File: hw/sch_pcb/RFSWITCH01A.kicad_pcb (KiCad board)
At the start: 2 copper layers, 40.1 x 40.1 mm, 31 parts, among them J1 HEADER_2x03_PARALLEL, J10 SMA, J11 HEADER_2x01_PARALLEL, J12 HEADER_2x01_PARALLEL, J2 HEADER_2x01_PARALLEL, J3 SMA, J4 SMA, J5 HEADER_2x01_PARALLEL, J6 HEADER_2x01_PARALLEL, J7 HEADER_2x01_PARALLEL, J8 HEADER_2x01_PARALLEL, J9 SMA, M1 HOLE, M2 HOLE, M3 HOLE, M4 HOLE, U1 TPS22945DCKR, U2 SPF5189Z, U3 PE4259, U4 PE4259

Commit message: Edit PCB
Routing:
- net GND: track 0.00 -> 2.03 mm
- net (no net): track 2.03 -> 0.00 mm
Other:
- board text added: "IN 3V3"
- board text added: "POWER"
- board text added: "RX/TX1"
- board text added: "RX/TX2"
- board text removed: "POWER IN"
- board text removed: "RX/TX-1"
- board text removed: "RX/TX-2"
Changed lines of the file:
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@@
     (pad "2" thru_hole circle (at -2.54 -2.54) (size 2.74 2.74) (drill 1.7) (layers *.Cu *.Mask)
       (net 2 "GND"))
-    (model "${KISYS3DMOD}/Connector_Coaxial.3dshapes/SMB_Jack_Vertical.wrl"
-      (offset (xyz 0 0 0))
+    (model "${KISYS3DMOD_MLAB}/MCX_TE_1330126-1_Vertical.step"
+      (offset (xyz 0 0 5.2))
       (scale (xyz 1 1 1))
       (rotate (xyz 0 0 0))
@@
     (property "Sheet name" "")
     (attr through_hole)
-    (fp_text reference "J3" (at -5.08 -0.635 90) (layer "F.SilkS")
+    (fp_text reference "J3" (at -5.08 0 90) (layer "F.SilkS")
       (effects (font (size 1 1) (thickness 0.15)))
     )
@@
     (pad "2" thru_hole circle (at 2.54 -2.54) (size 2.74 2.74) (drill 1.7) (layers *.Cu *.Mask)
       (net 2 "GND"))
-    (model "${KISYS3DMOD}/Connector_Coaxial.3dshapes/SMB_Jack_Vertical.wrl"
-      (offset (xyz 0 0 0))
+    (model "${KISYS3DMOD_MLAB}/MCX_TE_1330126-1_Vertical.step"
+      (offset (xyz 0 0 5.2))
       (scale (xyz 1 1 1))
       (rotate (xyz 0 0 0))
@@
     (pad "2" thru_hole circle (at -2.54 -2.54) (size 2.74 2.74) (drill 1.7) (layers *.Cu *.Mask)
       (net 2 "GND"))
-    (model "${KISYS3DMOD}/Connector_Coaxial.3dshapes/SMB_Jack_Vertical.wrl"
-      (offset (xyz 0 0 0))
+    (model "${KISYS3DMOD_MLAB}/MCX_TE_1330126-1_Vertical.step"
+      (offset (xyz 0 0 5.2))
       (scale (xyz 1 1 1))
       (rotate (xyz 0 0 0))
@@
     (property "Sheet name" "")
     (attr through_hole)
-    (fp_text reference "J4" (at -5.08 1 90) (layer "F.SilkS")
+    (fp_text reference "J4" (at -5.08 0 90) (layer "F.SilkS")
       (effects (font (size 1 1) (thickness 0.15)))
     )
@@
     (pad "2" thru_hole circle (at 2.54 2.54) (size 2.74 2.74) (drill 1.7) (layers *.Cu *.Mask)
       (net 2 "GND"))
-    (model "${KISYS3DMOD}/Connector_Coaxial.3dshapes/SMB_Jack_Vertical.wrl"
-      (offset (xyz 0 0 0))
+    (model "${KISYS3DMOD_MLAB}/MCX_TE_1330126-1_Vertical.step"
+      (offset (xyz 0 0 5.2))
       (scale (xyz 1 1 1))
       (rotate (xyz 0 0 0))
@@
   )
   (gr_line (start 28.702 -12.7) (end 28.956 -12.446) (layer "F.SilkS") (width 0.15))
-  (gr_line (start 13.335 -23.495) (end 13.97 -22.86) (layer "F.SilkS") (width 0.15))
   (gr_line (start 9.8552 -14.605) (end 11.663391 -14.605) (layer "F.SilkS") (width 0.15))
   (gr_line (start 15.387609 -14.605) (end 19.791391 -14.605) (layer "F.SilkS") (width 0.15))
+  (gr_line (start 11.663391 -14.605) (end 10.795 -15.24) (layer "F.SilkS") (width 0.15))
   (gr_circle (center 14.986 -14.605) (end 15.113 -14.986) (layer "F.SilkS") (width 0.15))
   (gr_line (start 20.066 -10.668) (end 20.066 -12.7) (layer "F.SilkS") (width 0.15))
   (gr_line (start 9.8552 -26.035) (end 11.43 -26.035) (layer "F.SilkS") (width 0.15))
   (gr_circle (center 22.098 -17.145) (end 22.352 -17.526) (layer "F.SilkS") (width 0.15))
+  (gr_line (start 13.97 -24.13) (end 13.335 -23.495) (layer "F.SilkS") (width 0.15))
   (gr_line (start 11.43 -19.05) (end 16.51 -19.05) (layer "F.SilkS") (width 0.15))
   (gr_circle (center 20.193 -14.605) (end 20.32 -14.986) (layer "F.SilkS") (width 0.15))
   (gr_line (start 27.686 -12.446) (end 27.686 -13.208) (layer "F.SilkS") (width 0.15))
-  (gr_line (start 10.795 -26.67) (end 11.43 -26.035) (layer "F.SilkS") (width 0.15))
+  (gr_line (start 13.97 -19.05) (end 14.605 -18.326453) (layer "F.SilkS") (width 0.15))
   (gr_line (start 14.986 -14.605) (end 12.446 -16.256) (layer "F.SilkS") (width 0.15))
   (gr_line (start 22.86 -11.938) (end 22.098 -12.7) (layer "F.SilkS") (width 0.15))
   (gr_circle (center 13.97 -17.145) (end 14.224 -17.526) (layer "F.SilkS") (width 0.15))
   (gr_line (start 13.97 -24.13) (end 13.97 -22.86) (layer "F.SilkS") (width 0.15))
-  (gr_line (start 1.016 -22.86) (end 1.016 -25.4) (layer "F.SilkS") (width 0.15))
+  (gr_line (start 13.97 -19.05) (end 13.335 -18.326453) (layer "F.SilkS") (width 0.15))
   (gr_line (start 11.43 -22.86) (end 11.43 -19.05) (layer "F.SilkS") (width 0.15))
   (gr_line (start 29.718 -11.684) (end 29.718 -10.922) (layer "F.SilkS") (width 0.15))
-  (gr_line (start 1.016 -25.4) (end 1.524 -25.908) (layer "F.SilkS") (width 0.15))
+  (gr_line (start 10.795 -15.24) (end 11.663391 -14.605) (layer "F.SilkS") (width 0.15))
+  (gr_line (start 13.97 -24.13) (end 14.605 -23.495) (layer "F.SilkS") (width 0.15))
   (gr_line (start 22.86 -26.035) (end 22.098 -25.273) (layer "F.SilkS") (width 0.15))
   (gr_line (start 22.098 -25.273) (end 22.098 -24.13) (layer "F.SilkS") (width 0.15))
   (gr_line (start 22.098 -12.7) (end 14.732 -12.7) (layer "F.SilkS") (width 0.15))
-  (gr_line (start 13.97 -22.86) (end 14.605 -23.495) (layer "F.SilkS") (width 0.15))
-  (gr_line (start 1.016 -17.78) (end 1.016 -15.24) (layer "F.SilkS") (width 0.15))
-  (gr_line (start 10.795 -25.4) (end 11.43 -26.035) (layer "F.SilkS") (width 0.15))
+  (gr_line (start 11.663391 -14.605) (end 10.795 -13.97) (layer "F.SilkS") (width 0.15))
   (gr_line (start 29.718 -11.684) (end 28.956 -12.446) (layer "F.SilkS") (width 0.15))
   (gr_circle (center 23.114 -14.605) (end 23.241 -14.986) (layer "F.SilkS") (width 0.15))
@@
   (gr_line (start 16.51 -19.05) (end 16.51 -22.86) (layer "F.SilkS") (width 0.15))
   (gr_line (start 13.97 -12.954) (end 13.97 -13.462) (layer "F.SilkS") (width 0.15))
-  (gr_line (start 11.43 -26.035) (end 10.795 -26.67) (layer "F.SilkS") (width 0.15))
   (gr_line (start 16.51 -27.94) (end 11.43 -27.94) (layer "F.SilkS") (width 0.15))
-  (gr_line (start 1.524 -14.732) (end 2.032 -14.732) (layer "F.SilkS") (width 0.15))
   (gr_line (start 22.606 -13.97) (end 22.098 -13.97) (layer "F.SilkS") (width 0.15))
   (gr_line (start 13.97 -13.462) (end 13.97 -12.954) (layer "F.SilkS") (width 0.15))
@@
   (gr_line (start 23.114 -16.256) (end 20.193 -14.605) (layer "F.SilkS") (width 0.15))
   (gr_line (start 26.416 -13.208) (end 22.86 -13.208) (layer "F.SilkS") (width 0.15))
-  (gr_line (start 1.524 -25.908) (end 2.032 -25.908) (layer "F.SilkS") (width 0.15))
   (gr_line (start 22.86 -13.208) (end 22.098 -13.97) (layer "F.SilkS") (width 0.15))
   (gr_line (start 16.51 -22.86) (end 11.43 -22.86) (layer "F.SilkS") (width 0.15))
+  (gr_line (start 9.8552 -26.035) (end 10.6426 -26.67) (layer "F.SilkS") (width 0.15))
   (gr_line (start 16.51 -24.13) (end 16.51 -27.94) (layer "F.SilkS") (width 0.15))
-  (gr_line (start 13.97 -22.86) (end 13.335 -23.495) (layer "F.SilkS") (width 0.15))
+  (gr_line (start 9.8552 -26.035) (end 10.6426 -25.4) (layer "F.SilkS") (width 0.15))
   (gr_line (start 11.43 -24.13) (end 16.51 -24.13) (layer "F.SilkS") (width 0.15))
   (gr_line (start 11.43 -27.94) (end 11.43 -24.13) (layer "F.SilkS") (width 0.15))
   (gr_line (start 30.7848 -26.035) (end 22.86 -26.035) (layer "F.SilkS") (width 0.15))
-  (gr_line (start 1.016 -15.24) (end 1.524 -14.732) (layer "F.SilkS") (width 0.15))
   (gr_line (start 28.702 -12.7) (end 28.194 -13.208) (layer "F.SilkS") (width 0.15))
   (gr_line (start 22.098 -13.97) (end 22.098 -13.462) (layer "F.SilkS") (width 0.15))
@@
     (effects (font (size 1.5 1.5) (thickness 0.3)) (justify mirror))
   )
-  (gr_text "RX/TX-1" (at 34.29 -31.369) (layer "F.SilkS")
+  (gr_text "RX/TX1" (at 34.29 -31.369) (layer "F.SilkS")
     (effects (font (size 1.5 1.5) (thickness 0.3)))
   )
@@
     (effects (font (size 1.5 1.5) (thickness 0.3)))
   )
-  (gr_text "3V3" (at 13.208 -1.27) (layer "F.SilkS")
+  (gr_text "IN 3V3" (at 13.208 -1.27) (layer "F.SilkS")
     (effects (font (size 1.5 1.5) (thickness 0.3)))
   )
@@
     (effects (font (size 1.5 1.5) (thickness 0.3)))
   )
-  (gr_text "POWER IN" (at 13.208 -8.89) (layer "F.SilkS")
+  (gr_text "POWER" (at 13.208 -8.89) (layer "F.SilkS")
     (effects (font (size 1.5 1.5) (thickness 0.3)))
   )
@@
     (effects (font (size 1.5 1.5) (thickness 0.3)))
   )
-  (gr_text "RFSWITCH01A" (at -2.159 -23.876 90) (layer "F.SilkS")
+  (gr_text "RFSWITCH01A" (at 20.32 -26.035 90) (layer "F.SilkS")
     (effects (font (size 1.5 1.5) (thickness 0.3)))
   )
@@
     (effects (font (size 1.5 1.5) (thickness 0.3)))
   )
-  (gr_text "RX/TX-2" (at 33.909 -20.32) (layer "F.SilkS")
+  (gr_text "RX/TX2" (at 34.29 -20.32) (layer "F.SilkS")
     (effects (font (size 1.5 1.5) (thickness 0.3)))
   )
@@
     (effects (font (size 1.5 1.5) (thickness 0.3)))
   )
-  (gr_text "MLAB.CZ" (at -5.207 -26.416 90) (layer "F.SilkS")
+  (gr_text "MLAB.CZ" (at 17.78 -26.67 90) (layer "F.SilkS")
     (effects (font (size 1.5 1.5) (thickness 0.3)))
   )
@@
     (effects (font (size 1.5 1.5) (thickness 0.3)))
   )
-  (segment (start 15.24 -12.192) (end 17.272 -12.192) (width 0.25) (layer "F.Cu") (net 0))
   (segment (start 13.208 -7.493) (end 13.42701 -7.71201) (width 0.8) (layer "F.Cu") (net 1))
   (segment (start 13.42701 -7.71201) (end 13.97 -8.255) (width 0.8) (layer "F.Cu") (net 1))
@@
   (segment (start 12.065 -11.43) (end 13.97 -11.43) (width 0.8) (layer "B.Cu") (net 1))
   (segment (start 17.78 -34.29) (end 17.78 -36.83) (width 0.4) (layer "B.Cu") (net 1))
+  (segment (start 15.24 -12.192) (end 17.272 -12.192) (width 0.25) (layer "F.Cu") (net 2))
   (via (at 11.049 -27.432) (size 0.4) (drill 0.15) (layers "F.Cu" "B.Cu") (net 2))
   (via (at 24.384 -21.844) (size 0.4) (drill 0.15) (layers "F.Cu" "B.Cu") (net 2))

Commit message: Předělávání PCB
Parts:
- removed J12: HEADER_2x01_PARALLEL, Mlab_Pin_Headers:Straight_2x01
- removed the J2 at (12.7, -35.6)
- added C10: 2p2, Mlab_R:SMD-0805, B.Cu at (48.0, -25.6)
- added C6: 1nF, Mlab_R:SMD-0805, B.Cu at (58.6, -19.1)
- added C7: 1nF, Mlab_R:SMD-0805, B.Cu at (50.2, -17.5)
- added C9: 2p2, Mlab_R:SMD-0805, B.Cu at (52.2, -25.6)
- added D2: BZV55C-3,6V, Diode_SMD:D_MiniMELF, B.Cu at (53.3, -10.2)
- added D3: BZV55C-3,6V, Diode_SMD:D_MiniMELF, B.Cu at (57.5, -22.0)
- added L4: 100nH, Mlab_R:SMD-0805, B.Cu at (50.8, -14.0)
- added L5: 100nH, Mlab_R:SMD-0805, B.Cu at (56.2, -14.0)
- added L6: 6n8, Mlab_R:SMD-0805, B.Cu at (49.2, -29.2)
- added R1: 10k, Mlab_R:SMD-0805, B.Cu at (15.7, -36.8)
- added R2: 10k, Mlab_R:SMD-0805, B.Cu at (29.2, -8.89)
- added R3: 10k, Mlab_R:SMD-0805, B.Cu at (24.4, -1.27)
- added R4: 10k, Mlab_R:SMD-0805, B.Cu at (20.6, -1.27)
- added R5: 10k, Mlab_R:SMD-0805, B.Cu at (17.8, -1.27)
- moved J5 2.54 mm to (25.4, -5.08)
- moved J6 2.54 mm to (12.7, -35.6)
- moved J4 2.54 mm to (27.9, -5.08)
- renumbered C6 to C8, J6 to J10, J3 to J2, J4 to J3, J7 to J4, J8 to J5, J11 to J6, J9 to J7, J10 to J8, J5 to J9, U4 to U2, U2 to U3, U3 to U4
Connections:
- C8 pad 2: Net-(C6-Pad2) -> Net-(C8-Pad2)
- J7 pad 1: /RX/TX_1 -> (no net)
- J8 pad 1: /RX/TX_2 -> (no net)
- U1 pad 4: /LNA_ON -> /SW1_CTRL
- U2 pad 1: /RX/TX_1 -> (no net)
- U2 pad 3: /RX/TX_2 -> (no net)
- U2 pad 5: Net-(U3-Pad5) -> (no net)
- U4 pad 1: /TX -> Net-(C8-Pad2)
- U4 pad 3: Net-(C6-Pad2) -> /TX
- U4 pad 5: Net-(U3-Pad5) -> (no net)
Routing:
- net +3V3: track 62.1 -> 48.5 mm
- net /LNA_ON: track 9.92 -> 0.00 mm, vias 1 -> 0
- net Net-(J6-Pad1): track 11.8 -> 17.3 mm
- net /SW2_#CTRL: track 17.2 -> 11.9 mm
- net Net-(C6-Pad2): track 3.50 -> 0.00 mm
- net /TX: track 19.4 -> 22.9 mm
- net Net-(U3-Pad5): track 3.18 -> 0.00 mm
- net Net-(C9-Pad1): track 0.00 -> 3.18 mm
- net /SW2_CTRL: track 14.3 -> 11.1 mm
- net /SW1_CTRL: track 16.8 -> 17.6 mm, vias 2 -> 3
- net GND: vias 219 -> 207
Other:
- board text removed: "ON"

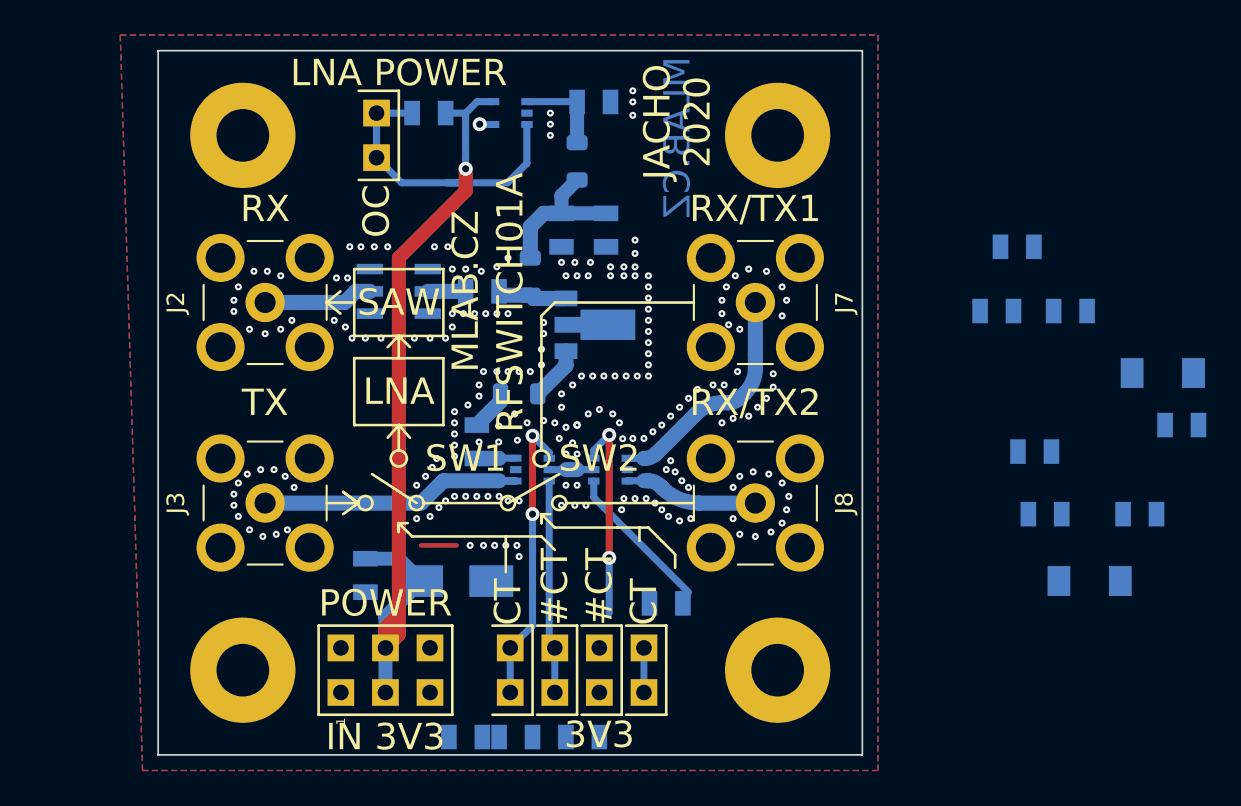
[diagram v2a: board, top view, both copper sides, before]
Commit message: Předělání PCB po změně schéma.
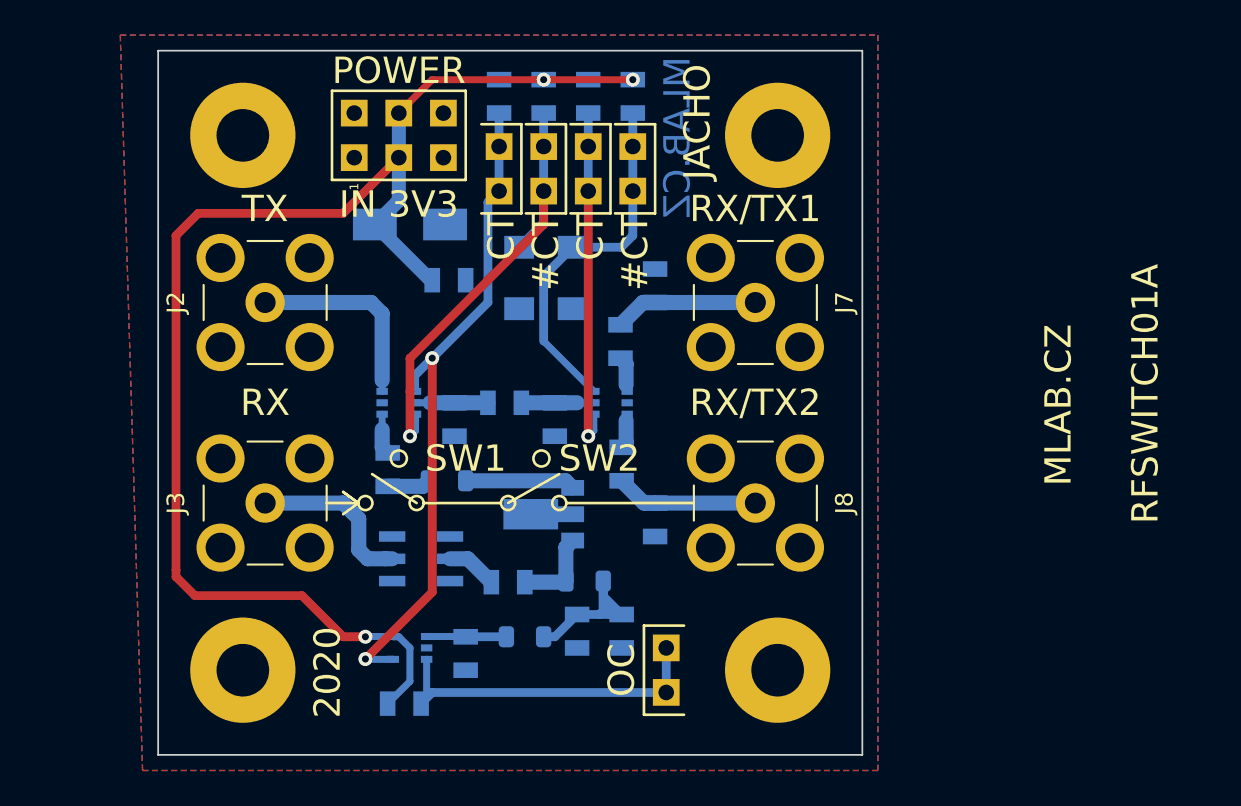
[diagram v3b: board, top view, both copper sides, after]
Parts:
- moved D3 37.1 mm to (20.8, -27.4), turned to -90 degrees
- moved R3 36.6 mm to (27.3, -37.8), turned to -90 degrees
- moved R5 36.6 mm to (19.7, -37.8), turned to 90 degrees
- moved R4 36.5 mm to (22.2, -37.8), turned to -90 degrees
- moved C9 35.6 mm to (17.1, -19.4), turned to -90 degrees
- moved J6 34.7 mm to (29.2, -5.08), turned to -90 degrees
- moved D2 34.2 mm to (23.9, -27.4), turned to -90 degrees
- moved R1 33.7 mm to (14.3, -3.17), turned to 0 degrees
- moved C6 32.3 mm to (26.6, -23.8), turned to 90 degrees
- moved C2 32.3 mm to (17.8, -6.03), turned to -90 degrees
- moved U1 31.0 mm to (14.6, -6.35)
- moved L6 30.5 mm to (20.0, -20.3), turned to 0 degrees
- moved J1 30.5 mm to (14.0, -35.6)
- moved R2 29.2 mm to (24.8, -37.8), turned to 90 degrees
- moved J4 28.8 mm to (24.8, -33.7)
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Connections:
- J2 pad 1: /RX -> /TX
- J3 pad 1: /TX -> /RX
- J7 pad 1: (no net) -> /RX/TX_1
- J8 pad 1: (no net) -> /RX/TX_2
- U2 pad 1: (no net) -> Net-(C6-Pad1)
- U2 pad 3: (no net) -> Net-(C7-Pad1)
- U2 pad 5: (no net) -> /RF_IN_OUT
- U4 pad 5: (no net) -> Net-(C9-Pad1)
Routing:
- net +3V3: track 48.5 -> 78.3 mm, vias 1 -> 3
- net /SW1_CTRL: track 17.6 -> 38.2 mm, vias 3 -> 2
- net /SW1_#CTRL: track 12.2 -> 26.7 mm, vias 0 -> 1
- net /TX: track 22.9 -> 11.4 mm
- net /SW2_#CTRL: track 11.9 -> 20.8 mm, vias 2 -> 0
- net /SW2_CTRL: track 11.1 -> 19.8 mm, vias 0 -> 1
- net /RX/TX_1: track 13.4 -> 8.21 mm
- net /RF_IN_OUT: track 0.00 -> 4.13 mm
- net /RX: track 6.23 -> 9.60 mm
- net Net-(L3-Pad1): track 3.10 -> 6.26 mm
- net Net-(C3-Pad1): track 8.68 -> 11.4 mm
- net Net-(C8-Pad2): track 0.00 -> 2.34 mm
- net Net-(J6-Pad1): track 17.3 -> 19.4 mm
- net GND: track 2.03 -> 0.00 mm, vias 207 -> 0
- net Net-(C6-Pad1): track 0.00 -> 1.66 mm
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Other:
- board text removed: "3V3"
- board text removed: "LNA"
- board text removed: "LNA POWER"
- board text removed: "SAW"

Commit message: Layout improvement #8.
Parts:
- moved C1 20.3 mm to (10.5, -7.98), turned to 90 degrees
- moved J6 7.79 mm to (21.6, -3.45), turned to 0 degrees
- moved C3 3.30 mm to (26.1, -4.67), turned to 0 degrees
- moved D3 2.17 mm to (18.7, -27.6), turned to 180 degrees
- moved R1 1.22 mm to (15.5, -3.25)
- moved D2 1.11 mm to (24.9, -27.9)
- moved L3 0.97 mm to (17.7, -16.0)
- moved C4 0.81 mm to (26.1, -6.71), turned to 0 degrees
- moved L2 0.58 mm to (24.3, -9.65), turned to 135 degrees
- moved L5 0.48 mm to (29.1, -13.7)
- moved D1 0.48 mm to (14.3, -30.9)
- moved L4 0.47 mm to (29.0, -27.0)
- moved C6 0.33 mm to (26.9, -23.7)
- moved C8 0.32 mm to (13.6, -16.7), turned to 135 degrees
- moved C7 0.27 mm to (26.9, -16.8)
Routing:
- net Net-(J6-Pad1): track 19.4 -> 9.31 mm
- net Net-(C3-Pad1): track 11.4 -> 7.35 mm
- net +3V3: track 78.3 -> 74.8 mm
- net /SW1_#CTRL: track 26.7 -> 29.0 mm
- net /TX: track 11.4 -> 9.87 mm
- net /SW2_#CTRL: track 20.8 -> 19.3 mm
- net /SW1_CTRL: track 38.2 -> 37.4 mm

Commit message: Edit PCB
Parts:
- moved D3 2.69 mm to (21.3, -27.9), turned to -90 degrees
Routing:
- net /SW1_#CTRL: track 29.0 -> 26.0 mm
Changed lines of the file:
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@@
   )
   (module "Diode_SMD:D_MiniMELF" (layer "B.Cu")
-    (at 18.6664 -27.5844 180)
+    (at 21.336 -27.912 -90)
     (descr "Diode Mini-MELF (SOD-80)")
     (tags "Diode Mini-MELF (SOD-80)")
@@
     (property "Sheet file" "D:/MLAB_G/Modules_zvlast/RFSWITCH01/hw/sch_pcb/RFSWITCH01A.kicad_sch")
     (attr smd)
-    (fp_text reference "D3" (at 0 2) (layer "B.SilkS")
-      (effects (font (size 1 1) (thickness 0.15)) (justify mirror))
-    )
-    (fp_text value "BZV55C-3,6V" (at 0 -1.75) (layer "B.Fab") hide
-      (effects (font (size 1 1) (thickness 0.15)) (justify mirror))
-    )
-    (fp_text user "${REFERENCE}" (at -3.048 0) (layer "B.Fab")
+    (fp_text reference "D3" (at 0 2 -270) (layer "B.SilkS")
+      (effects (font (size 1 1) (thickness 0.15)) (justify mirror))
+    )
+    (fp_text value "BZV55C-3,6V" (at 0 -1.75 -270) (layer "B.Fab") hide
+      (effects (font (size 1 1) (thickness 0.15)) (justify mirror))
+    )
+    (fp_text user "${REFERENCE}" (at -3.048 0 -270) (layer "B.Fab")
       (effects (font (size 1 1) (thickness 0.15)) (justify mirror))
     )
@@
     (fp_line (start -0.75 0) (end -0.35 0) (layer "B.Fab") (width 0.1))
     (fp_line (start 1.65 -0.8) (end -1.65 -0.8) (layer "B.Fab") (width 0.1))
-    (pad "1" smd rect (at -1.75 0 180) (size 1.3 1.7) (layers "B.Cu" "B.Paste" "B.Mask")
+    (pad "1" smd rect (at -1.75 0 270) (size 1.3 1.7) (layers "B.Cu" "B.Paste" "B.Mask")
       (net 13 "/SW1_#CTRL") (pinfunction "K"))
-    (pad "2" smd rect (at 1.75 0 180) (size 1.3 1.7) (layers "B.Cu" "B.Paste" "B.Mask")
+    (pad "2" smd rect (at 1.75 0 270) (size 1.3 1.7) (layers "B.Cu" "B.Paste" "B.Mask")
       (net 2 "GND") (pinfunction "A"))
     (model "${KISYS3DMOD}/Diode_SMD.3dshapes/D_MiniMELF.wrl"
@@
     (effects (font (size 1.5 1.5) (thickness 0.3)))
   )
-  (gr_text "OC" (at 26.67 -5.08 90) (layer "F.SilkS")
+  (gr_text "OC" (at 25.908 -3.429) (layer "F.SilkS")
     (effects (font (size 1.5 1.5) (thickness 0.3)))
   )
@@
   (segment (start 14.605 -20.955) (end 14.605 -18.415) (width 0.5) (layer "F.Cu") (net 13))
   (via (at 14.605 -18.415) (size 0.8) (drill 0.4) (layers "F.Cu" "B.Cu") (net 13))
-  (segment (start 22.225 -30.579) (end 22.225 -32.385) (width 0.5) (layer "B.Cu") (net 13))
   (segment (start 14.92 -18.73) (end 14.605 -18.415) (width 0.4) (layer "B.Cu") (net 13))
-  (segment (start 21.1722 -29.5262) (end 20.4164 -28.7704) (width 0.5) (layer "B.Cu") (net 13))
   (segment (start 22.225 -34.925) (end 22.225 -32.385) (width 0.5) (layer "B.Cu") (net 13))
+  (segment (start 22.225 -32.385) (end 22.225 -30.551) (width 0.5) (layer "B.Cu") (net 13))
+  (segment (start 22.225 -30.551) (end 21.336 -29.662) (width 0.5) (layer "B.Cu") (net 13))
   (segment (start 22.225 -36.83) (end 22.225 -34.925) (width 0.5) (layer "B.Cu") (net 13))
-  (segment (start 20.828 -29.182) (end 21.1722 -29.5262) (width 0.5) (layer "B.Cu") (net 13))
-  (segment (start 21.1722 -29.5262) (end 22.225 -30.579) (width 0.5) (layer "B.Cu") (net 13))
-  (segment (start 20.4164 -28.7704) (end 20.4164 -27.5844) (width 0.5) (layer "B.Cu") (net 13))
   (segment (start 14.92 -19.67) (end 14.92 -18.73) (width 0.4) (layer "B.Cu") (net 13))
   (segment (start 24.765 -32.385) (end 24.765 -18.415) (width 0.5) (layer "F.Cu") (net 14))

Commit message: Silkscreen improvement  #6
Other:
- board text added: "1"
- board text added: "2"
- board text added: "3V3"
- board text added: "RX/TX"
- board text removed: "IN 3V3"
- board text removed: "RX/TX1"
- board text removed: "RX/TX2"
- board text removed: "SW1"
- board text removed: "SW2"
